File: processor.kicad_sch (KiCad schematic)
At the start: 14 parts, among them U3 RP2040

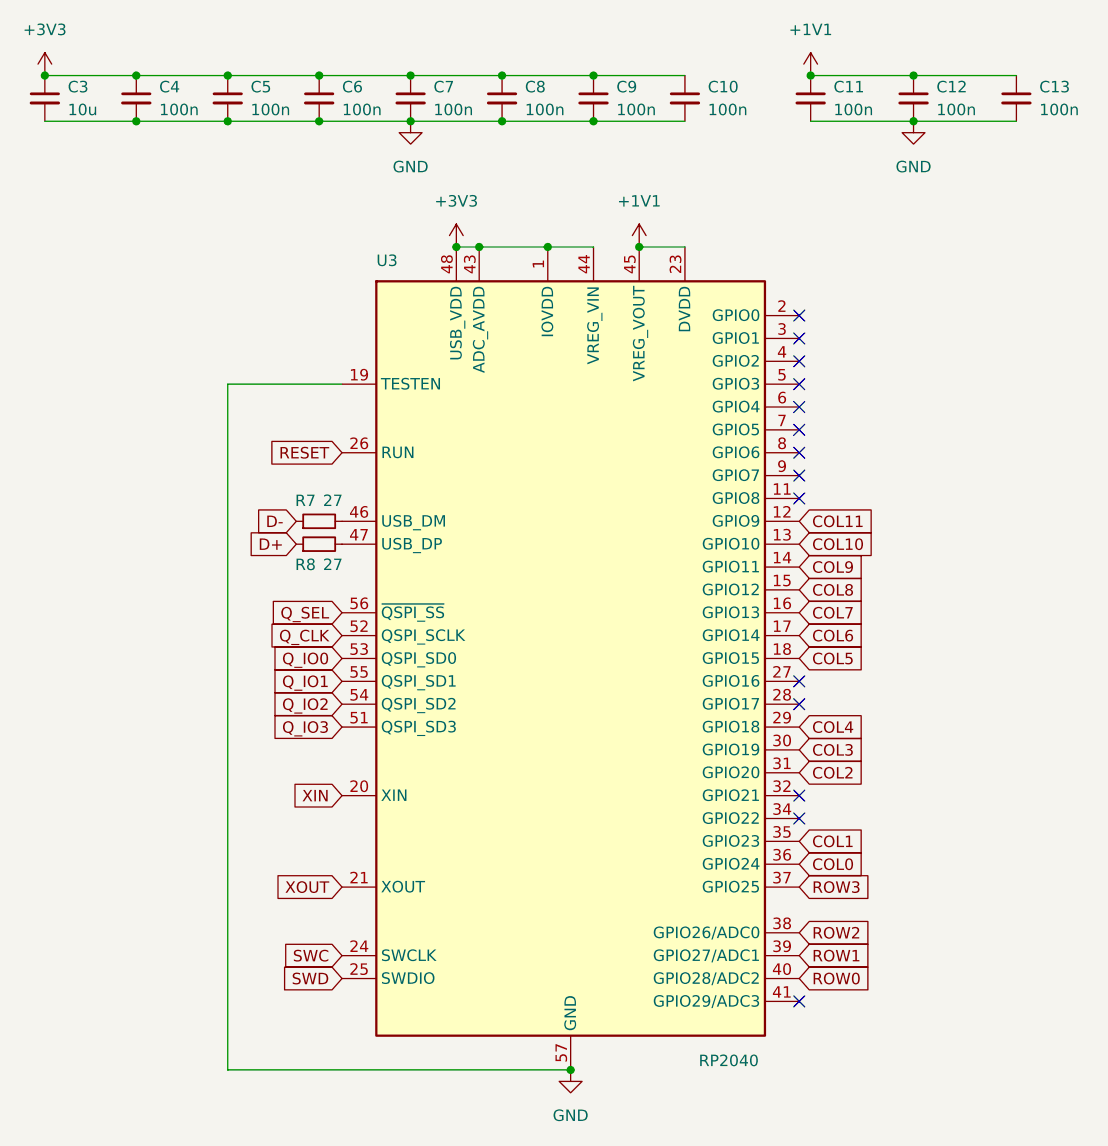
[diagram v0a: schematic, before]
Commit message: 4 layers
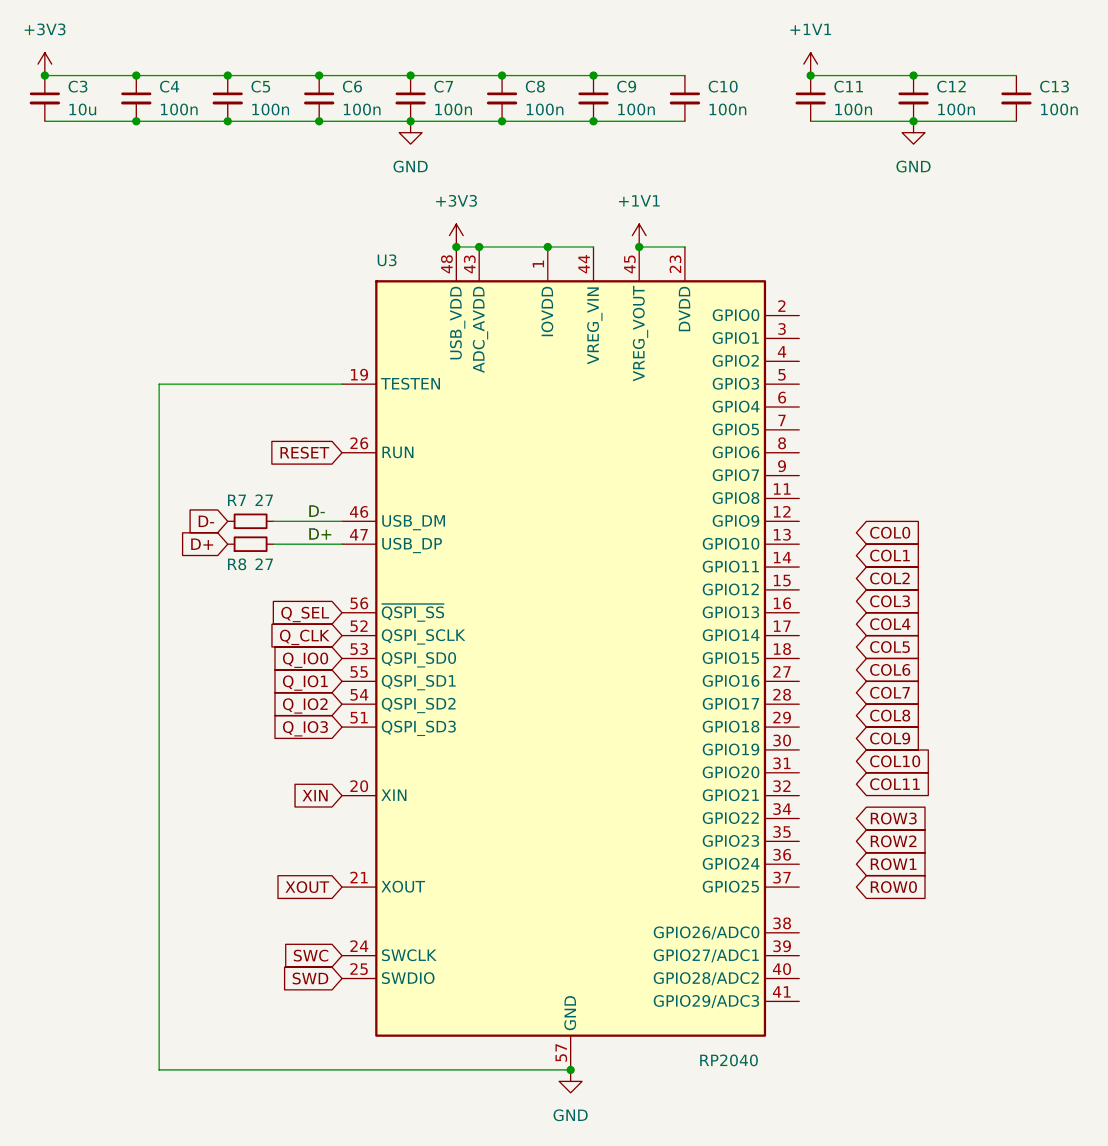
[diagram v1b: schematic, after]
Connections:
- net COL0: no longer U3.36 (GPIO24)
- net COL1: no longer U3.35 (GPIO23)
- net COL10: no longer U3.13 (GPIO10)
- net COL11: no longer U3.12 (GPIO9)
- net COL2: no longer U3.31 (GPIO20)
- net COL3: no longer U3.30 (GPIO19)
- net COL4: no longer U3.29 (GPIO18)
- net COL5: no longer U3.18 (GPIO15)
- net COL6: no longer U3.17 (GPIO14)
- net COL7: no longer U3.16 (GPIO13)
- net COL8: no longer U3.15 (GPIO12)
- net COL9: no longer U3.14 (GPIO11)
- net D+: now also R8.2, U3.47 (USB_DP)
- net D-: now also R7.2, U3.46 (USB_DM)
- net ROW0: no longer U3.40 (GPIO28/ADC2)
- net ROW1: no longer U3.39 (GPIO27/ADC1)
- net ROW2: no longer U3.38 (GPIO26/ADC0)
- net ROW3: no longer U3.37 (GPIO25)
- no-connect marks 14 -> 0
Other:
- moved on the sheet: R7, R8
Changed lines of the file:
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@@
 		(color 0 0 0 0)
 	)
-	(no_connect
-		(at 172.72 86.36)
-	)
-	(no_connect
-		(at 172.72 127)
-	)
-	(no_connect
-		(at 172.72 76.2)
-	)
-	(no_connect
-		(at 172.72 124.46)
-	)
-	(no_connect
-		(at 172.72 83.82)
-	)
-	(no_connect
-		(at 172.72 71.12)
-	)
-	(no_connect
-		(at 172.72 88.9)
-	)
-	(no_connect
-		(at 172.72 81.28)
-	)
-	(no_connect
-		(at 172.72 147.32)
-	)
-	(no_connect
-		(at 172.72 73.66)
-	)
-	(no_connect
-		(at 172.72 91.44)
-	)
-	(no_connect
-		(at 172.72 114.3)
-	)
-	(no_connect
-		(at 172.72 111.76)
-	)
-	(no_connect
-		(at 172.72 78.74)
-	)
 	(wire
 		(pts
@@
 	(wire
 		(pts
+			(xy 114.3 93.98) (xy 121.92 93.98)
+		)
+		(stroke
+			(width 0)
+			(type default)
+		)
+	)
+	(wire
+		(pts
 			(xy 173.99 44.45) (xy 185.42 44.45)
 		)
@@
 	(wire
 		(pts
-			(xy 121.92 78.74) (xy 109.22 78.74)
+			(xy 121.92 78.74) (xy 101.6 78.74)
 		)
 		(stroke
@@
 	(wire
 		(pts
-			(xy 109.22 154.94) (xy 147.32 154.94)
+			(xy 101.6 154.94) (xy 147.32 154.94)
 		)
 		(stroke
@@
 	(wire
 		(pts
-			(xy 109.22 78.74) (xy 109.22 154.94)
+			(xy 101.6 78.74) (xy 101.6 154.94)
 		)
 		(stroke
@@
 		)
 	)
+	(wire
+		(pts
+			(xy 114.3 96.52) (xy 121.92 96.52)
+		)
+		(stroke
+			(width 0)
+			(type default)
+		)
+	)
+	(label "D+"
+		(at 118.11 96.52 0)
+		(effects
+			(font
+				(size 1.27 1.27)
+			)
+			(justify bottom)
+		)
+	)
+	(label "D-"
+		(at 118.11 93.98 0)
+		(effects
+			(font
+				(size 1.27 1.27)
+			)
+			(justify bottom)
+		)
+	)
 	(global_label "COL6"
 		(shape input)
-		(at 172.72 106.68 0)
+		(at 179.07 110.49 0)
 		(fields_autoplaced yes)
 		(effects
@@
 		)
 		(property "Intersheetrefs" "${INTERSHEET_REFS}"
-			(at 180.5433 106.68 0)
+			(at 186.8933 110.49 0)
 			(effects
 				(font
@@
 	(global_label "COL4"
 		(shape input)
-		(at 172.72 116.84 0)
+		(at 179.07 105.41 0)
 		(fields_autoplaced yes)
 		(effects
@@
 		)
 		(property "Intersheetrefs" "${INTERSHEET_REFS}"
-			(at 180.5433 116.84 0)
+			(at 186.8933 105.41 0)
 			(effects
 				(font
@@
 	(global_label "COL10"
 		(shape input)
-		(at 172.72 96.52 0)
+		(at 179.07 120.65 0)
 		(fields_autoplaced yes)
 		(effects
@@
 		)
 		(property "Intersheetrefs" "${INTERSHEET_REFS}"
-			(at 181.7528 96.52 0)
+			(at 188.1028 120.65 0)
 			(effects
 				(font
@@
 	(global_label "COL11"
 		(shape input)
-		(at 172.72 93.98 0)
+		(at 179.07 123.19 0)
 		(fields_autoplaced yes)
 		(effects
@@
 		)
 		(property "Intersheetrefs" "${INTERSHEET_REFS}"
-			(at 181.7528 93.98 0)
+			(at 188.1028 123.19 0)
 			(effects
 				(font
@@
 	(global_label "COL2"
 		(shape input)
-		(at 172.72 121.92 0)
+		(at 179.07 100.33 0)
 		(fields_autoplaced yes)
 		(effects
@@
 		)
 		(property "Intersheetrefs" "${INTERSHEET_REFS}"
-			(at 180.5433 121.92 0)
+			(at 186.8933 100.33 0)
 			(effects
 				(font
@@
 	(global_label "D+"
 		(shape input)
-		(at 116.84 96.52 180)
+		(at 109.22 96.52 180)
 		(fields_autoplaced yes)
 		(effects
@@
 		)
 		(property "Intersheetrefs" "${INTERSHEET_REFS}"
-			(at 111.0124 96.52 0)
+			(at 103.3924 96.52 0)
 			(effects
 				(font
@@
 	(global_label "COL1"
 		(shape input)
-		(at 172.72 129.54 0)
+		(at 179.07 97.79 0)
 		(fields_autoplaced yes)
 		(effects
@@
 		)
 		(property "Intersheetrefs" "${INTERSHEET_REFS}"
-			(at 180.5433 129.54 0)
+			(at 186.8933 97.79 0)
 			(effects
 				(font
@@
 	(global_label "ROW0"
 		(shape input)
-		(at 172.72 144.78 0)
+		(at 179.07 134.62 0)
 		(fields_autoplaced yes)
 		(effects
@@
 		)
 		(property "Intersheetrefs" "${INTERSHEET_REFS}"
-			(at 180.9666 144.78 0)
+			(at 187.3166 134.62 0)
 			(effects
 				(font
@@
 	(global_label "COL3"
 		(shape input)
-		(at 172.72 119.38 0)
+		(at 179.07 102.87 0)
 		(fields_autoplaced yes)
 		(effects
@@
 		)
 		(property "Intersheetrefs" "${INTERSHEET_REFS}"
-			(at 180.5433 119.38 0)
+			(at 186.8933 102.87 0)
 			(effects
 				(font
@@
 	(global_label "ROW1"
 		(shape input)
-		(at 172.72 142.24 0)
+		(at 179.07 132.08 0)
 		(fields_autoplaced yes)
 		(effects
@@
 		)
 		(property "Intersheetrefs" "${INTERSHEET_REFS}"
-			(at 180.9666 142.24 0)
+			(at 187.3166 132.08 0)
 			(effects
 				(font
@@
 	(global_label "COL9"
 		(shape input)
-		(at 172.72 99.06 0)
+		(at 179.07 118.11 0)
 		(fields_autoplaced yes)
 		(effects
@@
 		)
 		(property "Intersheetrefs" "${INTERSHEET_REFS}"
-			(at 180.5433 99.06 0)
+			(at 186.8933 118.11 0)
 			(effects
 				(font
@@
 	(global_label "COL8"
 		(shape input)
-		(at 172.72 101.6 0)
+		(at 179.07 115.57 0)
 		(fields_autoplaced yes)
 		(effects
@@
 		)
 		(property "Intersheetrefs" "${INTERSHEET_REFS}"
-			(at 180.5433 101.6 0)
+			(at 186.8933 115.57 0)
 			(effects
 				(font
@@
 	(global_label "D-"
 		(shape input)
-		(at 116.84 93.98 180)
+		(at 109.22 93.98 180)
 		(fields_autoplaced yes)
 		(effects
@@
 		)
 		(property "Intersheetrefs" "${INTERSHEET_REFS}"
-			(at 111.0124 93.98 0)
+			(at 103.3924 93.98 0)
 			(effects
 				(font
@@
 	(global_label "COL0"
 		(shape input)
-		(at 172.72 132.08 0)
+		(at 179.07 95.25 0)
 		(fields_autoplaced yes)
 		(effects
@@
 		)
 		(property "Intersheetrefs" "${INTERSHEET_REFS}"
-			(at 180.5433 132.08 0)
+			(at 186.8933 95.25 0)
 			(effects
 				(font
@@
 	(global_label "ROW2"
 		(shape input)
-		(at 172.72 139.7 0)
+		(at 179.07 129.54 0)
 		(fields_autoplaced yes)
 		(effects
@@
 		)
 		(property "Intersheetrefs" "${INTERSHEET_REFS}"
-			(at 180.9666 139.7 0)
+			(at 187.3166 129.54 0)
 			(effects
 				(font
@@
 	(global_label "COL7"
 		(shape input)
-		(at 172.72 104.14 0)
+		(at 179.07 113.03 0)
 		(fields_autoplaced yes)
 		(effects
@@
 		)
 		(property "Intersheetrefs" "${INTERSHEET_REFS}"
-			(at 180.5433 104.14 0)
+			(at 186.8933 113.03 0)
 			(effects
 				(font
@@
 	(global_label "COL5"
 		(shape input)
-		(at 172.72 109.22 0)
+		(at 179.07 107.95 0)
 		(fields_autoplaced yes)
 		(effects
@@
 		)
 		(property "Intersheetrefs" "${INTERSHEET_REFS}"
-			(at 180.5433 109.22 0)
+			(at 186.8933 107.95 0)
 			(effects
 				(font
@@
 	(global_label "ROW3"
 		(shape input)
-		(at 172.72 134.62 0)
+		(at 179.07 127 0)
 		(fields_autoplaced yes)
 		(effects
@@
 		)
 		(property "Intersheetrefs" "${INTERSHEET_REFS}"
-			(at 180.9666 134.62 0)
+			(at 187.3166 127 0)
 			(effects
 				(font
@@
 	(symbol
 		(lib_id "Device:R_Small")
-		(at 119.38 96.52 90)
+		(at 111.76 96.52 90)
 		(unit 1)
 		(exclude_from_sim no)
@@
 		(dnp no)
 		(property "Reference" "R8"
-			(at 117.856 98.806 90)
+			(at 110.236 98.806 90)
 			(effects
 				(font
@@
 		)
 		(property "Value" "27"
-			(at 120.904 98.806 90)
+			(at 113.284 98.806 90)
 			(effects
 				(font
@@
 		)
 		(property "Footprint" "Library:R_0402_1005Metric"
-			(at 119.38 96.52 0)
+			(at 111.76 96.52 0)
 			(effects
 				(font
@@
 		)
 		(property "Datasheet" "~"
-			(at 119.38 96.52 0)
+			(at 111.76 96.52 0)
 			(effects
 				(font
@@
 		)
 		(property "Description" "Resistor, small symbol"
-			(at 119.38 96.52 0)
+			(at 111.76 96.52 0)
 			(effects
 				(font
@@
 	(symbol
 		(lib_id "Device:R_Small")
-		(at 119.38 93.98 90)
+		(at 111.76 93.98 90)
 		(unit 1)
 		(exclude_from_sim no)
@@
 		(dnp no)
 		(property "Reference" "R7"
-			(at 117.856 91.694 90)
+			(at 110.236 91.694 90)
 			(effects
 				(font
@@
 		)
 		(property "Value" "27"
-			(at 120.904 91.694 90)
+			(at 113.284 91.694 90)
 			(effects
 				(font
@@
 		)
 		(property "Footprint" "Library:R_0402_1005Metric"
-			(at 119.38 93.98 0)
+			(at 111.76 93.98 0)
 			(effects
 				(font
@@
 		)
 		(property "Datasheet" "~"
-			(at 119.38 93.98 0)
+			(at 111.76 93.98 0)
 			(effects
 				(font
@@
 		)
 		(property "Description" "Resistor, small symbol"
-			(at 119.38 93.98 0)
-			(effects
-				(font
+			(at 111.76 93.98 0)
+			(effects
+				(font

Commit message: routed matrix
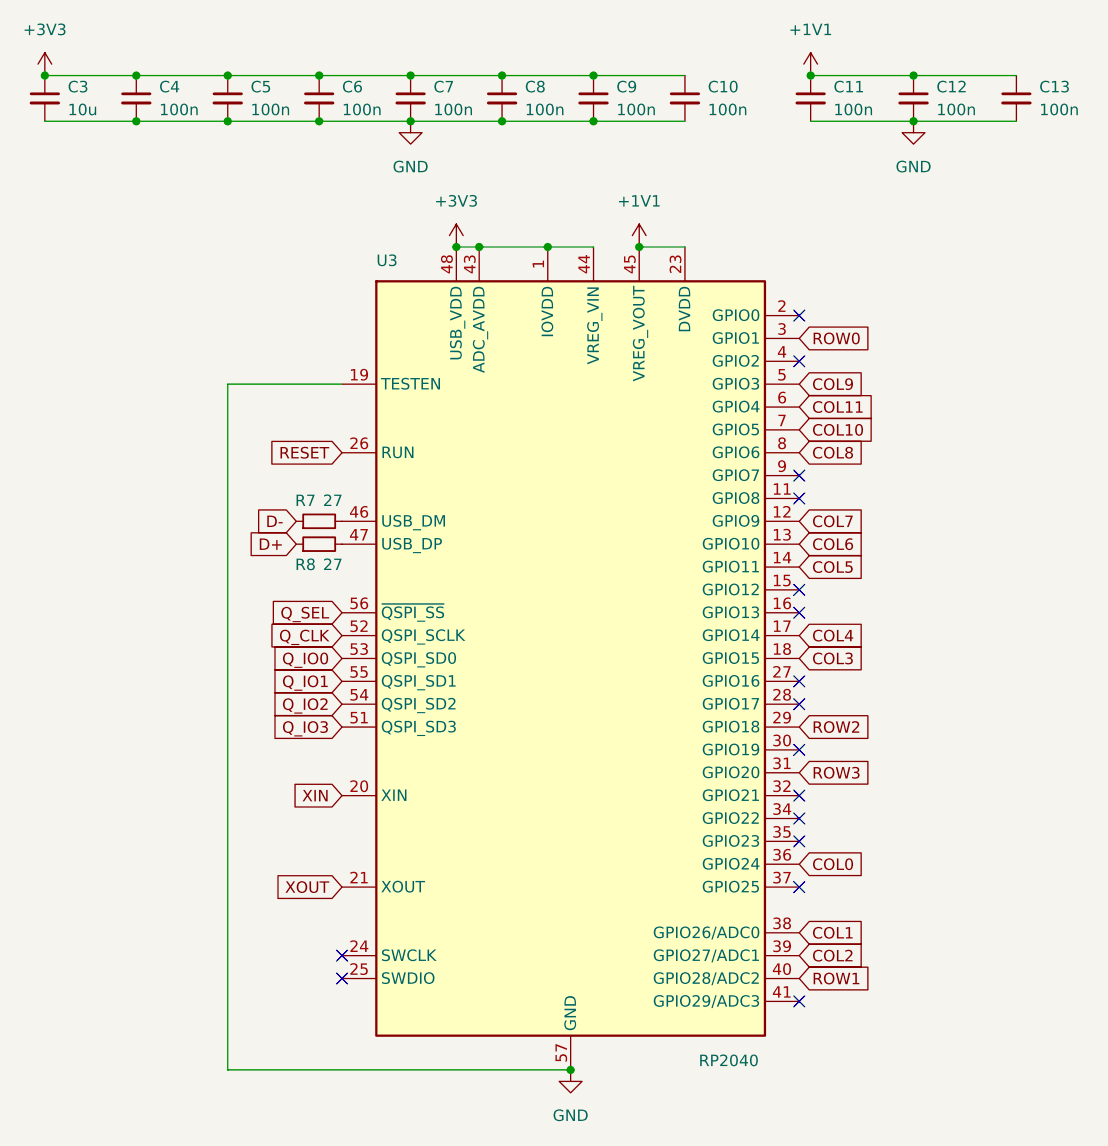
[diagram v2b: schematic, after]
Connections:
- net COL0: now also U3.36 (GPIO24)
- net COL1: now also U3.38 (GPIO26/ADC0)
- net COL10: now also U3.7 (GPIO5)
- net COL11: now also U3.6 (GPIO4)
- net COL2: now also U3.39 (GPIO27/ADC1)
- net COL3: now also U3.18 (GPIO15)
- net COL4: now also U3.17 (GPIO14)
- net COL5: now also U3.14 (GPIO11)
- net COL6: now also U3.13 (GPIO10)
- net COL7: now also U3.12 (GPIO9)
- net COL8: now also U3.8 (GPIO6)
- net COL9: now also U3.5 (GPIO3)
- net D+: no longer R8.2, U3.47 (USB_DP)
- net D-: no longer R7.2, U3.46 (USB_DM)
- net ROW0: now also U3.3 (GPIO1)
- net ROW1: now also U3.40 (GPIO28/ADC2)
- net ROW2: now also U3.29 (GPIO18)
- net ROW3: now also U3.31 (GPIO20)
- net SWC: no longer names the net of U3.24 (SWCLK)
- net SWD: no longer names the net of U3.25 (SWDIO)
- new net: R7.2, U3.46 (USB_DM)
- new net: R8.2, U3.47 (USB_DP)
- no-connect marks 0 -> 16
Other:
- moved on the sheet: R7, R8

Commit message: BOM
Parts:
- C10, C11, C12, C13, C4, C5, C6, C7, C8, C9: LCSC (none) -> C1525
- C3: LCSC (none) -> C1691
- R7, R8: LCSC (none) -> C25100
- U3: LCSC (none) -> C2040
